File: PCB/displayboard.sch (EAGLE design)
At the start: 9 parts

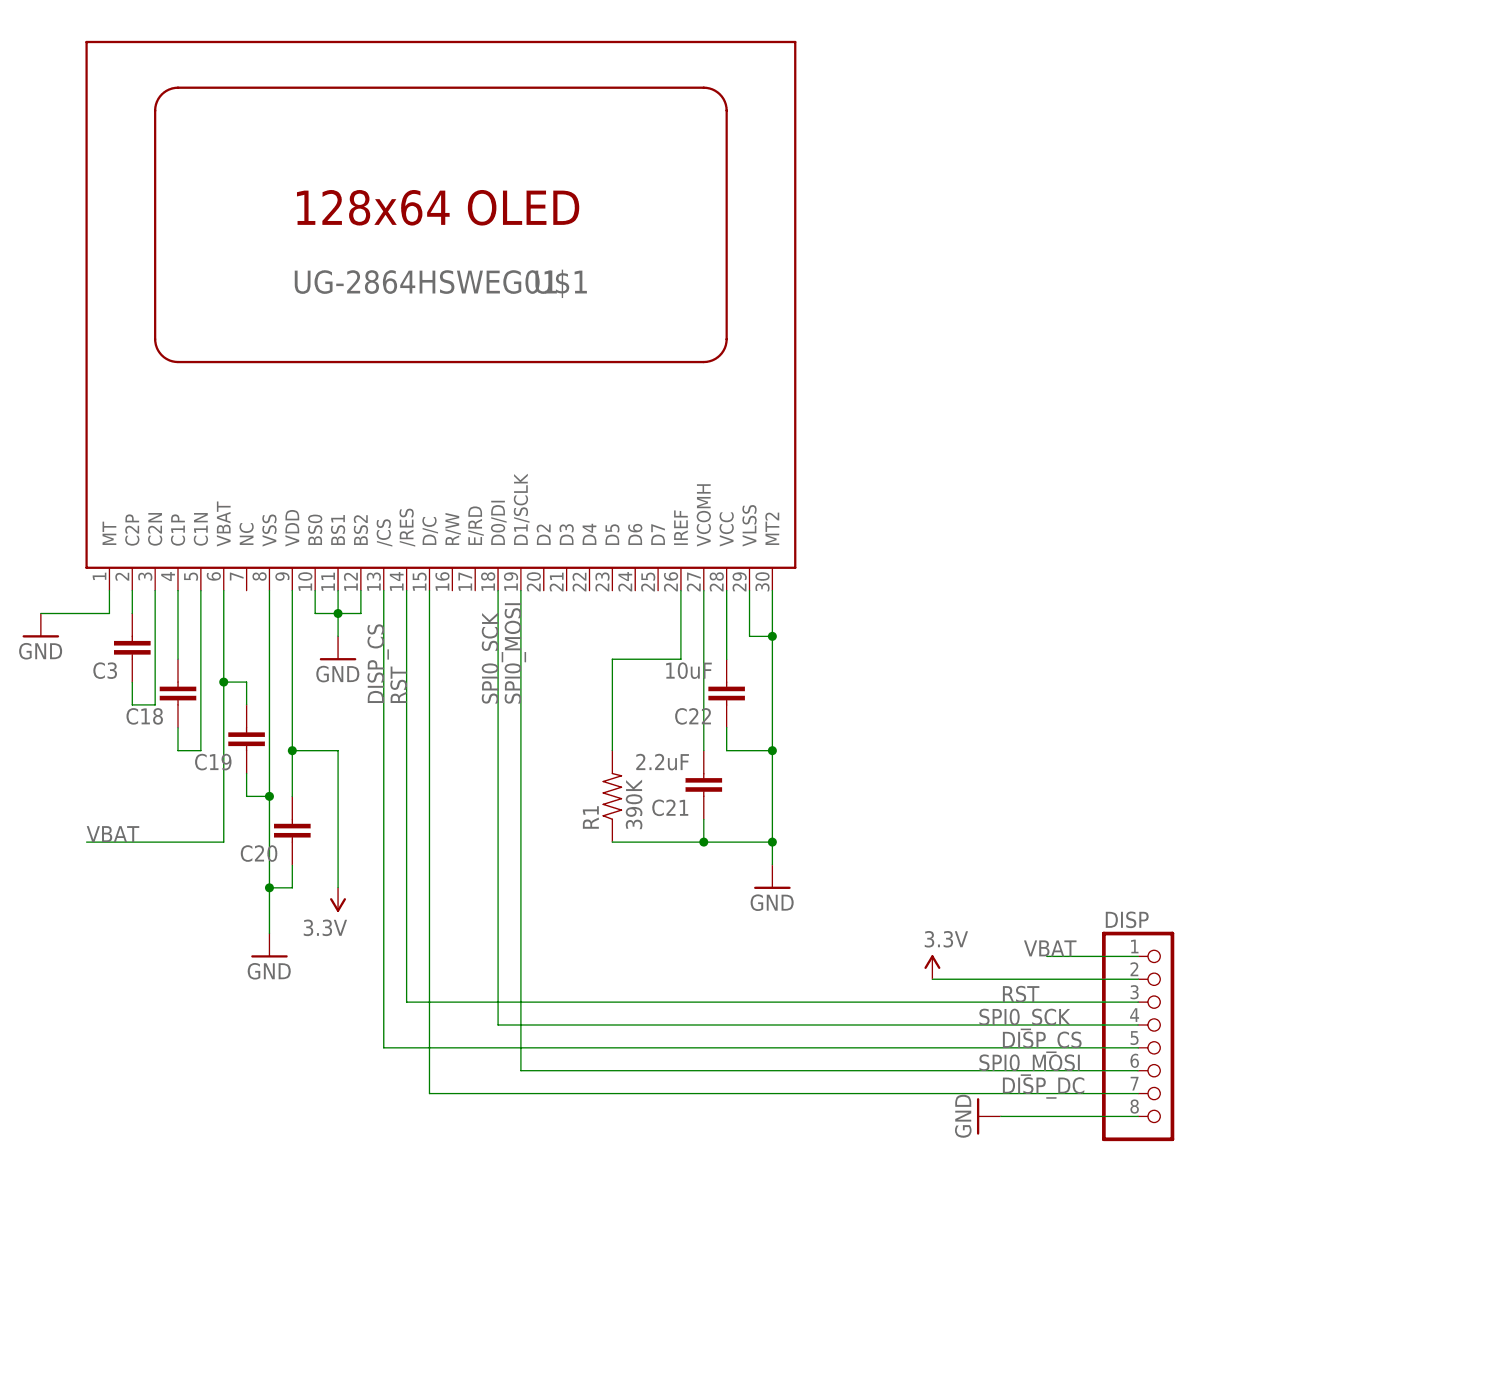
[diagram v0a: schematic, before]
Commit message: Displayboard completed.. Need to check connector width
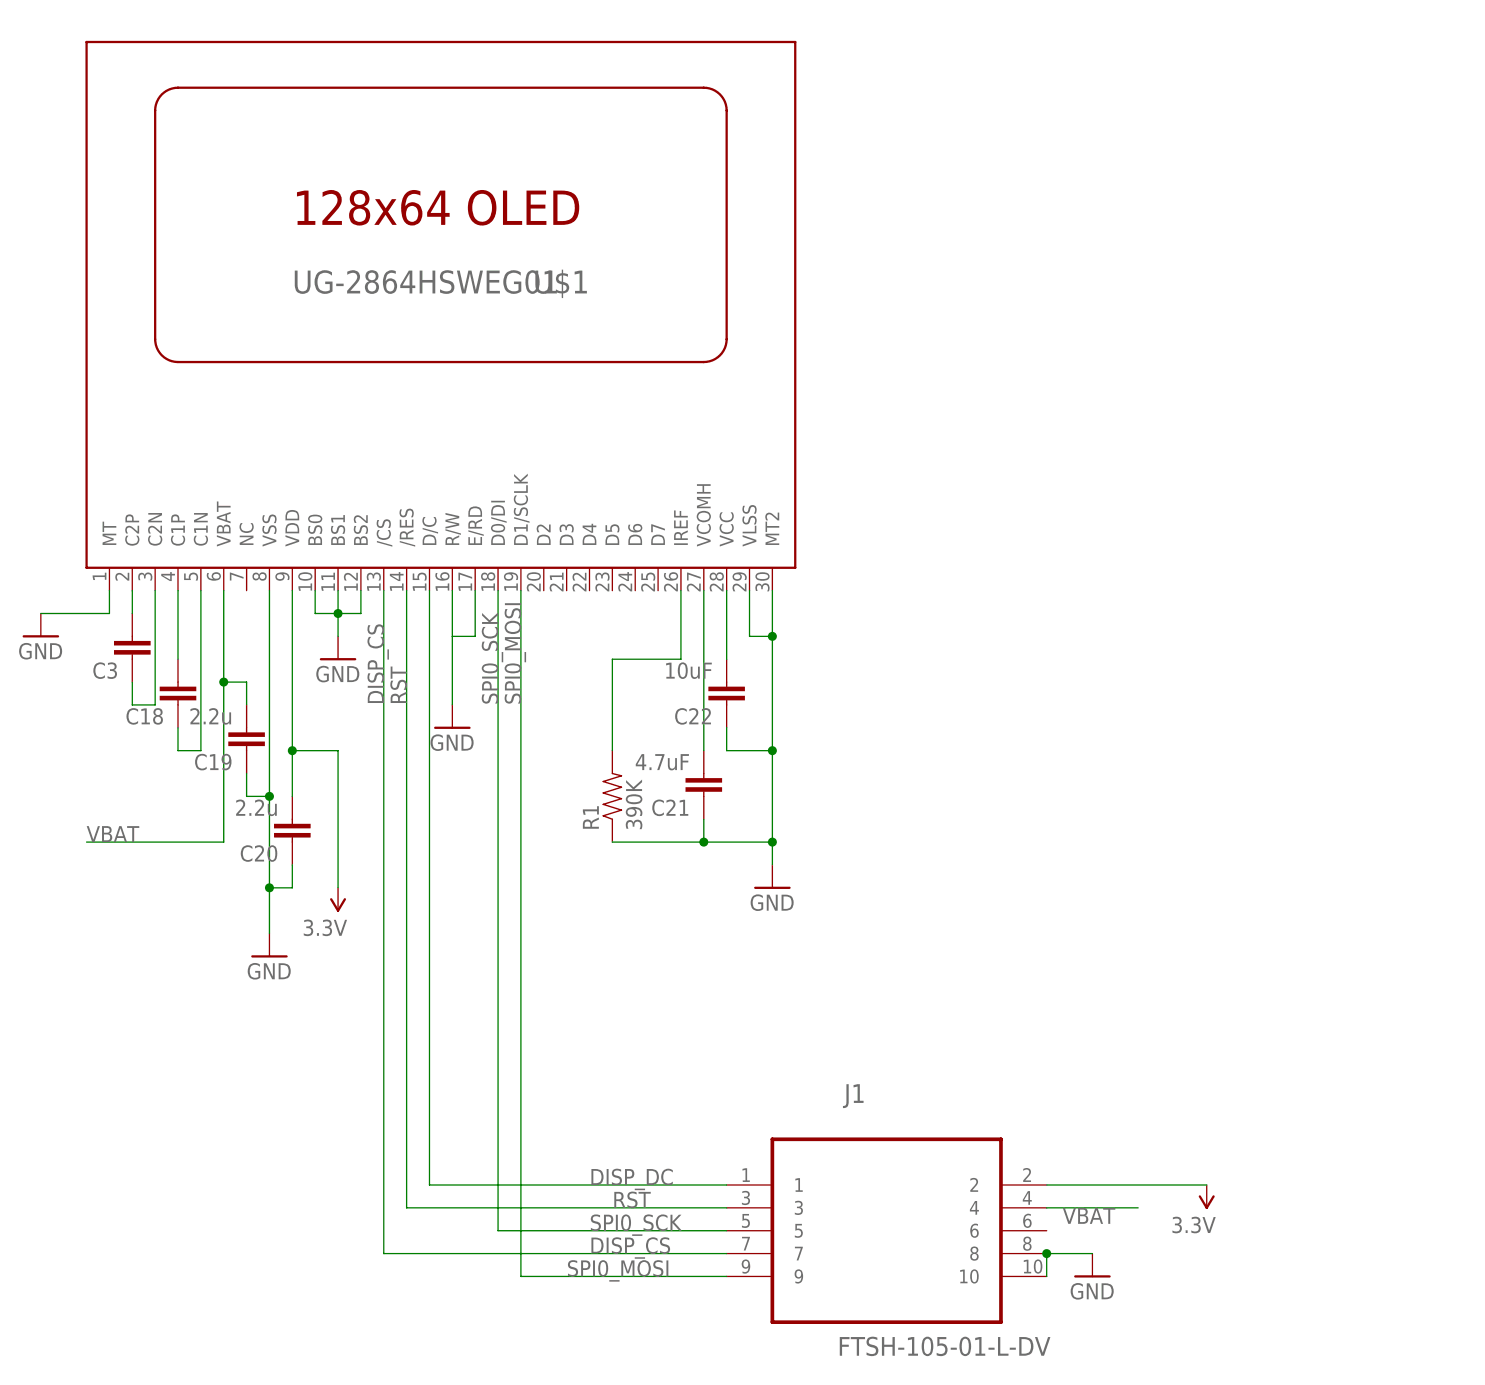
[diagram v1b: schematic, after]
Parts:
- removed DISP: (no value), microbuilder:JST_8PIN
- added J1: FTSH-105-01-L-DV, SAMTEC-HTSW-FTxx_By_element14_Batch_1:FTSH-105-01-L-DV
- C19, C20: value (none) -> 2.2u
- C21: value 2.2uF -> 4.7uF
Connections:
- net 3.3V: now also J1.2; no longer DISP.2
- net DISP_CS: now also J1.7; no longer DISP.5
- net DISP_DC: now also J1.1; no longer DISP.7
- net GND: now also J1.10, J1.8, U$1.E/RD, U$1.R/W; no longer DISP.8
- net RST: now also J1.3; no longer DISP.3
- net SPI0_MOSI: now also J1.9; no longer DISP.6
- net SPI0_SCK: now also J1.5; no longer DISP.4
- net VBAT: now also J1.4; no longer DISP.1
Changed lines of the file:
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@@
 <?xml version="1.0" encoding="utf-8"?>
 <!DOCTYPE eagle SYSTEM "eagle.dtd">
-<eagle version="6.5.0">
+<eagle version="6.4">
 <drawing>
 <settings>
@@
 </classes>
 <parts>
-<part name="DISP" library="microbuilder" deviceset="JST_8PIN" device=""/>
-<part name="SUPPLY1" library="SparkFun-Aesthetics" deviceset="3.3V" device=""/>
-<part name="GND4" library="SparkFun-Aesthetics" deviceset="GND" device=""/>
 <part name="U$1" library="adafruit" deviceset="UG-2864HSWEG01" device=""/>
 <part name="GND3" library="SparkFun-Aesthetics" deviceset="GND" device=""/>
 <part name="C3" library="SparkFun-Capacitors" deviceset="CAP" device="0805"/>
 <part name="C18" library="SparkFun-Capacitors" deviceset="CAP" device="0805"/>
-<part name="C19" library="SparkFun-Capacitors" deviceset="CAP" device="0805"/>
-<part name="C20" library="SparkFun-Capacitors" deviceset="CAP" device="0805"/>
-<part name="C21" library="SparkFun-Capacitors" deviceset="CAP" device="0805" value="2.2uF"/>
+<part name="C19" library="SparkFun-Capacitors" deviceset="CAP" device="0805" value="2.2u"/>
+<part name="C20" library="SparkFun-Capacitors" deviceset="CAP" device="0805" value="2.2u"/>
+<part name="C21" library="SparkFun-Capacitors" deviceset="CAP" device="0805" value="4.7uF"/>
 <part name="C22" library="SparkFun-Capacitors" deviceset="CAP" device="0805" value="10uF"/>
 <part name="R1" library="SparkFun-Passives" deviceset="RESISTOR" device="0805-RES" value="390K"/>
@@
 <part name="GND30" library="SparkFun-Aesthetics" deviceset="GND" device=""/>
 <part name="SUPPLY2" library="SparkFun-Aesthetics" deviceset="3.3V" device=""/>
+<part name="SUPPLY3" library="SparkFun-Aesthetics" deviceset="3.3V" device=""/>
+<part name="GND2" library="SparkFun-Aesthetics" deviceset="GND" device=""/>
+<part name="J1" library="SAMTEC-HTSW-FTxx_By_element14_Batch_1" deviceset="FTSH-105-01-L-DV" device=""/>
+<part name="GND4" library="SparkFun-Aesthetics" deviceset="GND" device=""/>
 </parts>
 <sheets>
@@
 </plain>
 <instances>
-<instance part="DISP" gate="G$1" x="101.6" y="7.62"/>
-<instance part="SUPPLY1" gate="G$1" x="76.2" y="15.24"/>
-<instance part="GND4" gate="1" x="81.28" y="0" rot="R270"/>
 <instance part="U$1" gate="G$1" x="20.32" y="83.82"/>
 <instance part="GND3" gate="1" x="-22.86" y="53.34"/>
@@
 <instance part="GND30" gate="1" x="2.54" y="17.78"/>
 <instance part="SUPPLY2" gate="G$1" x="10.16" y="25.4" rot="R180"/>
+<instance part="SUPPLY3" gate="G$1" x="106.68" y="-7.62" rot="R180"/>
+<instance part="GND2" gate="1" x="93.98" y="-17.78"/>
+<instance part="J1" gate="A" x="71.12" y="-10.16"/>
+<instance part="GND4" gate="1" x="22.86" y="43.18"/>
 </instances>
 <busses>
@@
 <nets>
 <net name="GND" class="0">
-<segment>
-<pinref part="DISP" gate="G$1" pin="8"/>
-<wire x1="99.06" y1="0" x2="83.82" y2="0" width="0.1524" layer="91"/>
-<pinref part="GND4" gate="1" pin="GND"/>
-</segment>
 <segment>
 <pinref part="U$1" gate="G$1" pin="MT"/>
@@
 <pinref part="GND29" gate="1" pin="GND"/>
 </segment>
+<segment>
+<pinref part="J1" gate="A" pin="8"/>
+<pinref part="J1" gate="A" pin="10"/>
+<wire x1="88.9" y1="-15.24" x2="88.9" y2="-17.78" width="0.1524" layer="91"/>
+<junction x="88.9" y="-15.24"/>
+<wire x1="88.9" y1="-15.24" x2="93.98" y2="-15.24" width="0.1524" layer="91"/>
+<pinref part="GND2" gate="1" pin="GND"/>
+</segment>
+<segment>
+<pinref part="U$1" gate="G$1" pin="E/RD"/>
+<wire x1="25.4" y1="58.42" x2="25.4" y2="53.34" width="0.1524" layer="91"/>
+<pinref part="U$1" gate="G$1" pin="R/W"/>
+<wire x1="22.86" y1="53.34" x2="22.86" y2="58.42" width="0.1524" layer="91"/>
+<wire x1="25.4" y1="53.34" x2="22.86" y2="53.34" width="0.1524" layer="91"/>
+<wire x1="22.86" y1="53.34" x2="22.86" y2="45.72" width="0.1524" layer="91"/>
+<pinref part="GND4" gate="1" pin="GND"/>
+</segment>
 </net>
 <net name="VBAT" class="0">
-<segment>
-<pinref part="DISP" gate="G$1" pin="1"/>
-<wire x1="99.06" y1="17.78" x2="88.9" y2="17.78" width="0.1524" layer="91"/>
-<label x="86.36" y="17.78" size="1.778" layer="95"/>
-</segment>
 <segment>
 <pinref part="U$1" gate="G$1" pin="VBAT"/>
@@
 <wire x1="-2.54" y1="30.48" x2="-17.78" y2="30.48" width="0.1524" layer="91"/>
 </segment>
+<segment>
+<pinref part="J1" gate="A" pin="4"/>
+<wire x1="88.9" y1="-10.16" x2="99.06" y2="-10.16" width="0.1524" layer="91"/>
+<label x="96.52" y="-10.16" size="1.778" layer="95" rot="R180"/>
+</segment>
 </net>
 <net name="3.3V" class="0">
-<segment>
-<pinref part="DISP" gate="G$1" pin="2"/>
-<pinref part="SUPPLY1" gate="G$1" pin="3.3V"/>
-<wire x1="99.06" y1="15.24" x2="76.2" y2="15.24" width="0.1524" layer="91"/>
-</segment>
 <segment>
 <pinref part="C20" gate="G$1" pin="2"/>
@@
 <junction x="5.08" y="40.64"/>
 </segment>
+<segment>
+<pinref part="J1" gate="A" pin="2"/>
+<pinref part="SUPPLY3" gate="G$1" pin="3.3V"/>
+<wire x1="88.9" y1="-7.62" x2="106.68" y2="-7.62" width="0.1524" layer="91"/>
+</segment>
 </net>
 <net name="SPI0_MOSI" class="0">
 <segment>
-<pinref part="DISP" gate="G$1" pin="6"/>
-<label x="81.28" y="5.08" size="1.778" layer="95"/>
 <pinref part="U$1" gate="G$1" pin="D1/SCLK"/>
 <label x="30.48" y="45.72" size="1.778" layer="95" rot="R90"/>
-<wire x1="99.06" y1="5.08" x2="30.48" y2="5.08" width="0.1524" layer="91"/>
-<wire x1="30.48" y1="5.08" x2="30.48" y2="58.42" width="0.1524" layer="91"/>
+<wire x1="30.48" y1="58.42" x2="30.48" y2="-17.78" width="0.1524" layer="91"/>
+<wire x1="53.34" y1="-17.78" x2="30.48" y2="-17.78" width="0.1524" layer="91"/>
+<label x="35.56" y="-17.78" size="1.778" layer="95"/>
+<pinref part="J1" gate="A" pin="9"/>
 </segment>
 </net>
 <net name="DISP_CS" class="0">
 <segment>
-<pinref part="DISP" gate="G$1" pin="5"/>
-<label x="83.82" y="7.62" size="1.778" layer="95"/>
 <pinref part="U$1" gate="G$1" pin="/CS"/>
 <label x="15.24" y="45.72" size="1.778" layer="95" rot="R90"/>
-<wire x1="99.06" y1="7.62" x2="15.24" y2="7.62" width="0.1524" layer="91"/>
-<wire x1="15.24" y1="7.62" x2="15.24" y2="58.42" width="0.1524" layer="91"/>
+<wire x1="15.24" y1="58.42" x2="15.24" y2="-15.24" width="0.1524" layer="91"/>
+<label x="38.1" y="-15.24" size="1.778" layer="95"/>
+<pinref part="J1" gate="A" pin="7"/>
+<wire x1="15.24" y1="-15.24" x2="53.34" y2="-15.24" width="0.1524" layer="91"/>
 </segment>
 </net>
 <net name="DISP_DC" class="0">
 <segment>
-<pinref part="DISP" gate="G$1" pin="7"/>
-<label x="83.82" y="2.54" size="1.778" layer="95"/>
 <pinref part="U$1" gate="G$1" pin="D/C"/>
-<wire x1="20.32" y1="58.42" x2="20.32" y2="2.54" width="0.1524" layer="91"/>
-<wire x1="20.32" y1="2.54" x2="99.06" y2="2.54" width="0.1524" layer="91"/>
+<wire x1="20.32" y1="58.42" x2="20.32" y2="-7.62" width="0.1524" layer="91"/>
+<label x="38.1" y="-7.62" size="1.778" layer="95"/>
+<pinref part="J1" gate="A" pin="1"/>
+<wire x1="20.32" y1="-7.62" x2="53.34" y2="-7.62" width="0.1524" layer="91"/>
 </segment>
 </net>
@@
 <pinref part="U$1" gate="G$1" pin="/RES"/>
 <label x="17.78" y="45.72" size="1.778" layer="95" rot="R90"/>
-<wire x1="17.78" y1="58.42" x2="17.78" y2="12.7" width="0.1524" layer="91"/>
-<label x="83.82" y="12.7" size="1.778" layer="95"/>
-<pinref part="DISP" gate="G$1" pin="3"/>
-<wire x1="17.78" y1="12.7" x2="99.06" y2="12.7" width="0.1524" layer="91"/>
+<wire x1="17.78" y1="58.42" x2="17.78" y2="-10.16" width="0.1524" layer="91"/>
+<label x="40.64" y="-10.16" size="1.778" layer="95"/>
+<pinref part="J1" gate="A" pin="3"/>
+<wire x1="17.78" y1="-10.16" x2="53.34" y2="-10.16" width="0.1524" layer="91"/>
 </segment>
 </net>
@@
 <pinref part="U$1" gate="G$1" pin="D0/DI"/>
 <label x="27.94" y="45.72" size="1.778" layer="95" rot="R90"/>
-<wire x1="27.94" y1="58.42" x2="27.94" y2="10.16" width="0.1524" layer="91"/>
-<pinref part="DISP" gate="G$1" pin="4"/>
-<label x="81.28" y="10.16" size="1.778" layer="95"/>
-<wire x1="27.94" y1="10.16" x2="99.06" y2="10.16" width="0.1524" layer="91"/>
-</segment>
-</net>
+<wire x1="27.94" y1="58.42" x2="27.94" y2="-12.7" width="0.1524" layer="91"/>
+<wire x1="53.34" y1="-12.7" x2="27.94" y2="-12.7" width="0.1524" layer="91"/>
+<label x="38.1" y="-12.7" size="1.778" layer="95"/>
+<pinref part="J1" gate="A" pin="5"/>
+</segment>
+</net>

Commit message: Final version of both PCBs.. Send to OSHPark
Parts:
- removed C19: 2.2u, SparkFun-Capacitors:CAP0805
- removed C21: 4.7uF, SparkFun-Capacitors:CAP0805
- added C1: 1uF, SparkFun-Capacitors:CAP0805
- added C5: 4.7uF, SparkFun-Capacitors:CAP0805
- added DISP_SW: (no value), SparkFun-Electromechanical:TAC_SWITCHKSA_SEALED
- C2: value (none) -> 1uF
- C3: value (none) -> 2.2u
- renumbered C18 to C2, C20 to C4, C22 to C6
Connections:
- new net DISP_SW: DISP_SW.1, J1.8
- net GND: now also C3.1, C5.1, DISP_SW.3, U$1.NC0, U$1.NC1; no longer C19.1, C21.1, J1.8, U$1.BS0, U$1.E/RD, U$1.MT, U$1.MT2, U$1.R/W
- net N$25: now also C1.2; no longer C3.2
- net N$27: now also C1.1; no longer C3.1
- net N$28: now also C5.2; no longer C21.2
- net SPI0_MOSI: now also U$1.D1/MOSI; no longer U$1.D1/SCLK
- net SPI0_SCK: now also U$1.D0/SCLK; no longer U$1.D0/DI
- net VBAT: now also C3.2; no longer C19.2
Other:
- moved on the sheet: C3, R1
